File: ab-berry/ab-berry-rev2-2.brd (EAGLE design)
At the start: 58.4 x 61 mm, 74 parts, among them IC1 STM32F303CCT6, IC2 AT45DB161D-SU, Q1 BSS84, U1 LM1117MPX-3.3/NOPB or AP2114H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, U2 PRTR5V0U2X, X1 04-JST-B4B-XH-A, X2 04-JST-B4B-XH-A, X3 ABM7-8.000MHZ-D2Y-T

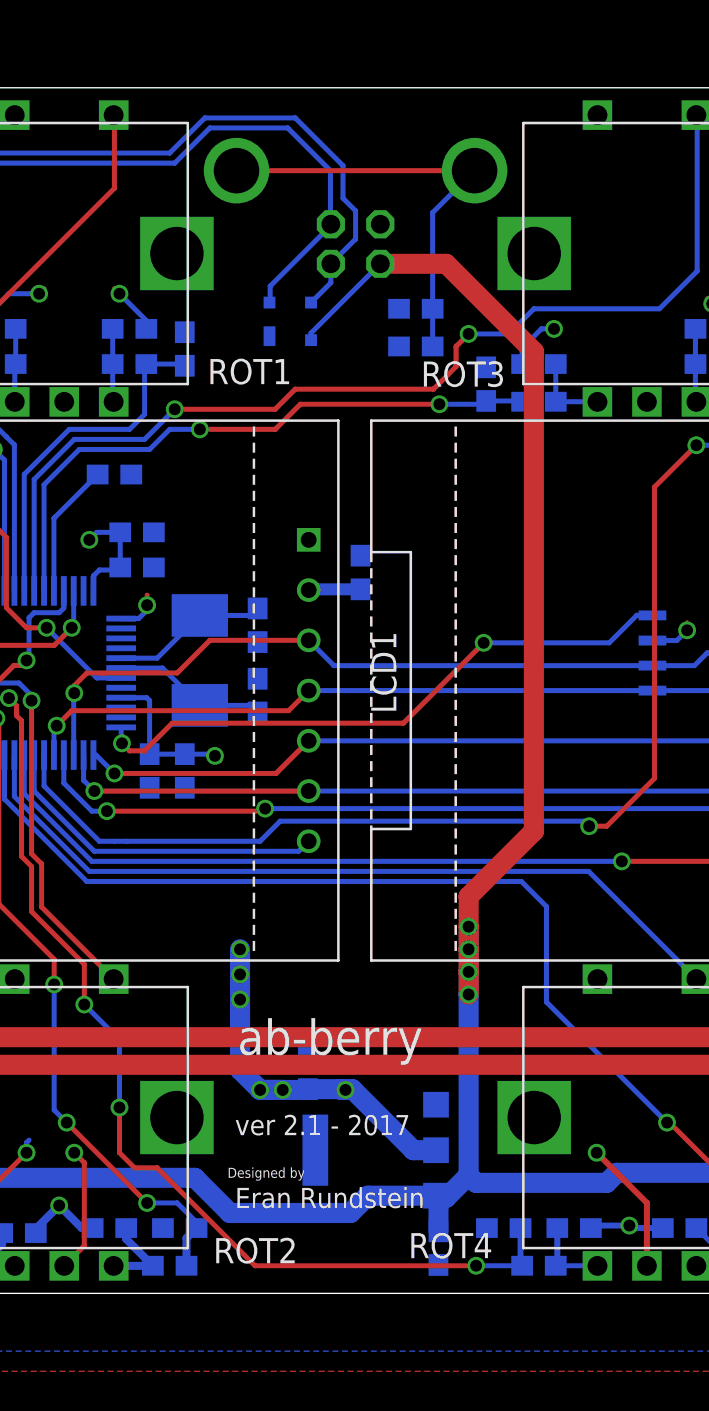
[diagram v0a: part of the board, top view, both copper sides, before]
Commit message: ab-berry: master jumper, phi branding, some macrofab attribs
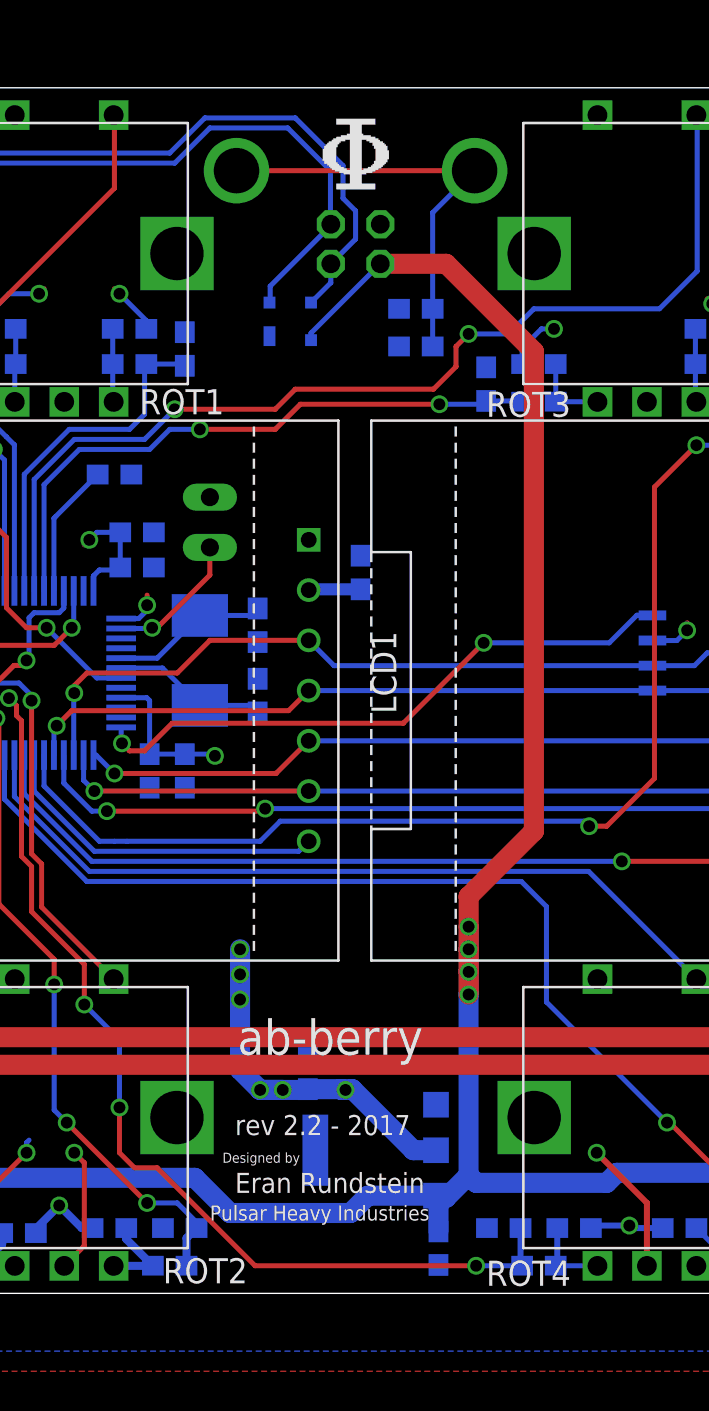
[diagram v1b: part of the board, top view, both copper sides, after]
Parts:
- added MASTER_EN: (no value), jumper:JP1
- renumbered JP2 to CAN_TERM
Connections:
- new net N$22: IC1.2, MASTER_EN.1
- net GND: now also MASTER_EN.2
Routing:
- net N$22: track 0.00 -> 7.00 mm, vias 0 -> 1
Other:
- board text added: "Pulsar Heavy Industries"
- board text added: "rev 2.2 - 2017"
- board text removed: "ver 2.1 - 2017"
